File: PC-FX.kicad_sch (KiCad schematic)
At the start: 60 parts, among them CN101 Conn_01x18_Socket, CN102 Conn_01x10_Pin, CN103 Conn_01x07_Pin, CN104 Conn_01x06_Pin, CN105 Conn_01x03_Socket, IC106 BA4510F, IC108 BA4510F, Q101 PNP

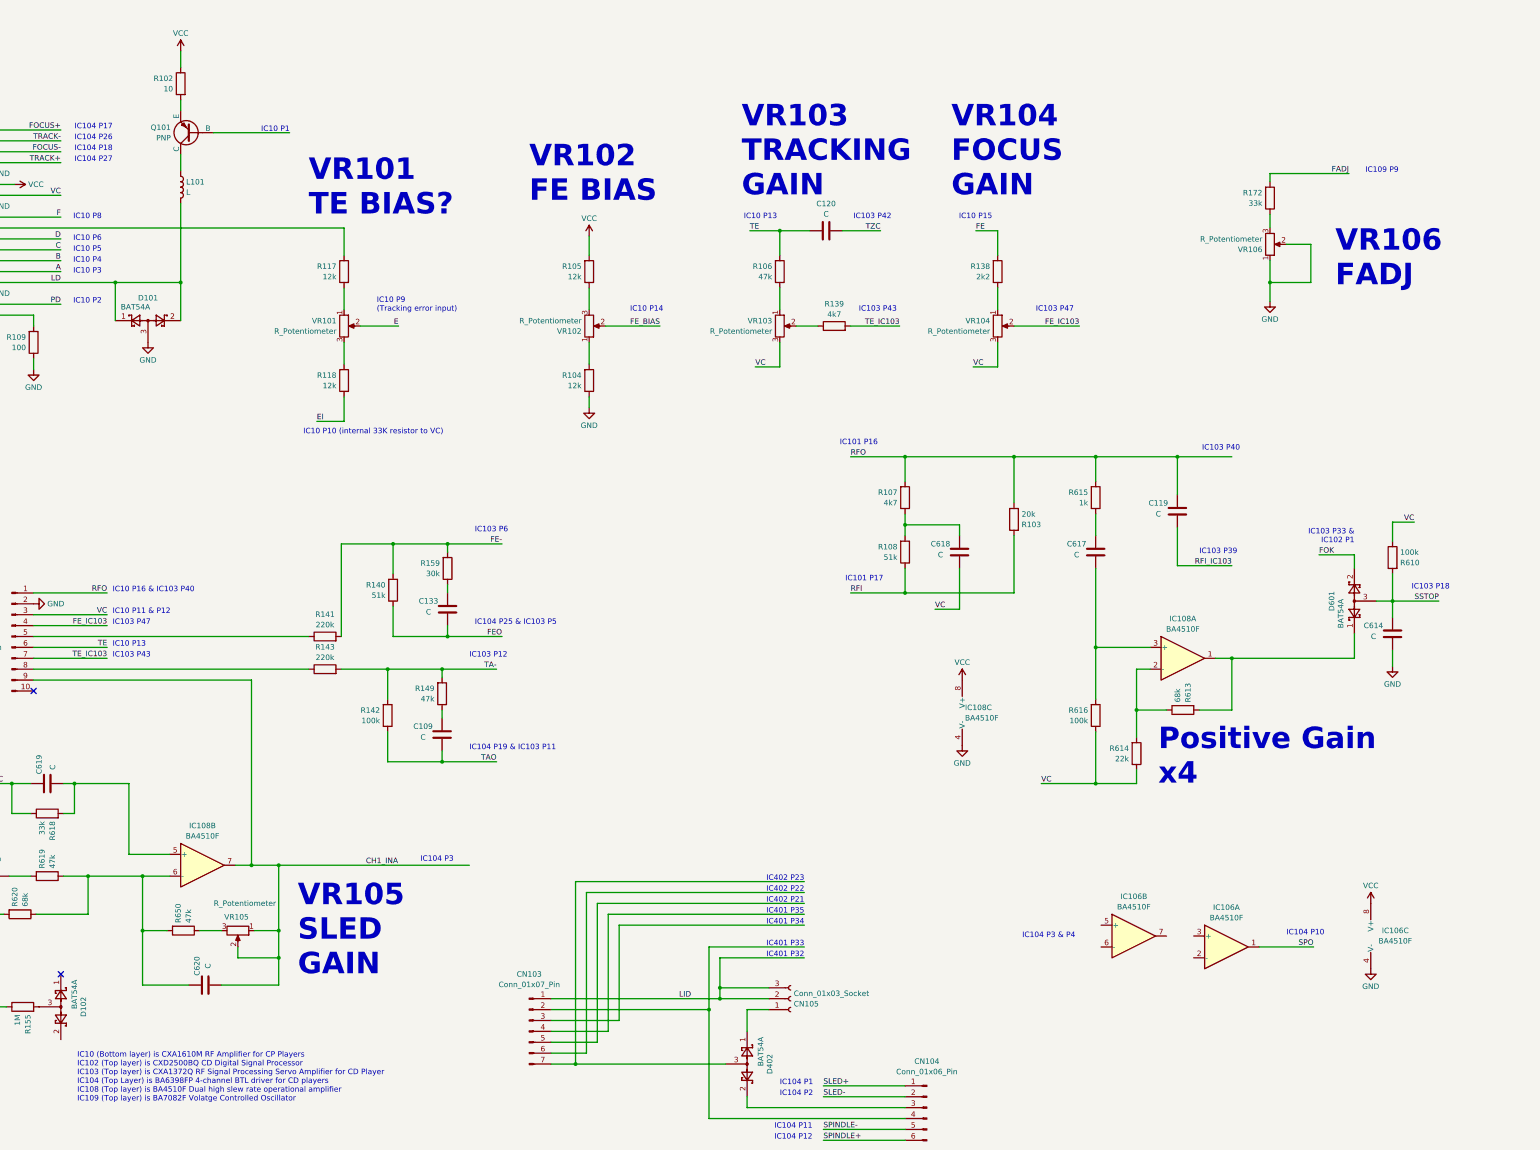
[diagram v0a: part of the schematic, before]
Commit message: Update that includes Frequency adjustment.
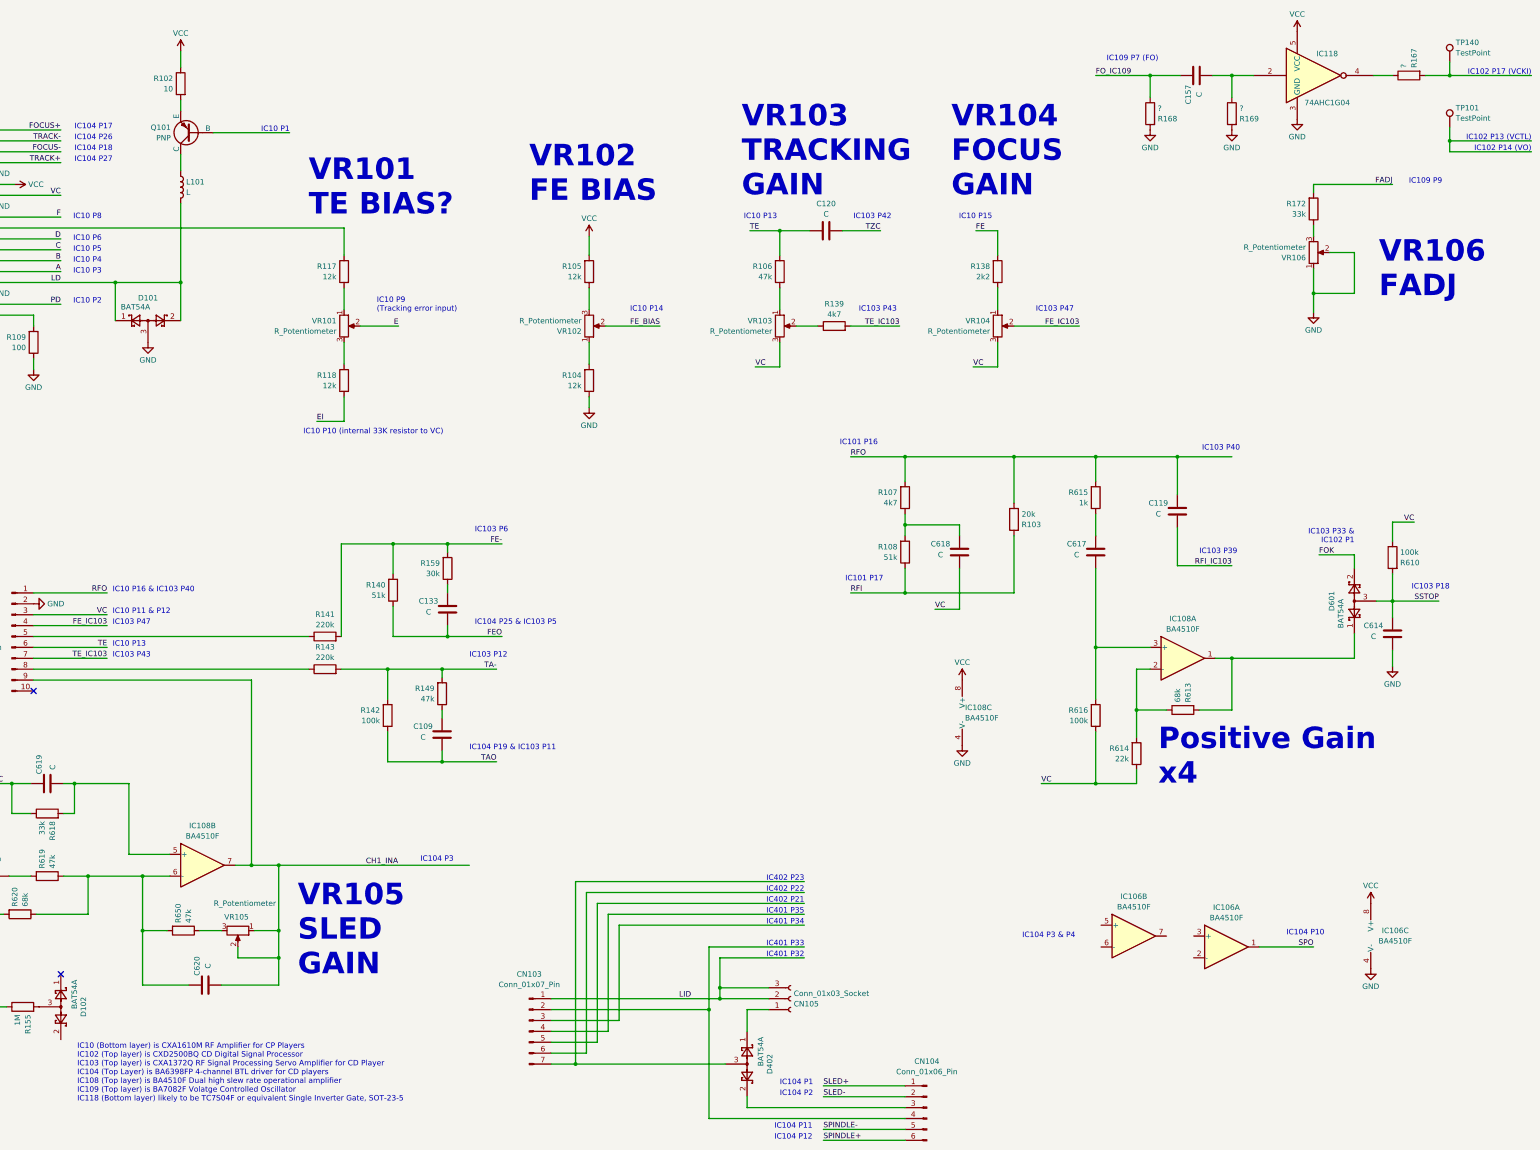
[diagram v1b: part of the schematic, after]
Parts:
- added C157: C, symbol Device:C
- added IC118: 74AHC1G04, symbol 74xGxx:74AHC1G04
- added R167, R168, R169: ?, symbol Device:R
- added TP101, TP140: TestPoint, symbol Connector:TestPoint
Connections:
- net GND: now also IC118.3 (GND), R168.2, R169.2
- net VCC: now also IC118.5 (VCC)
- new net: C157.2, IC118.2, R169.1
- new net: R167.2, TP140.1
- new net: IC118.4, R167.1
- new net FO_IC109: C157.1, R168.1
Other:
- note added: "IC10 (Bottom layer) is CXA1610M RF Amplifier for CP Players IC102 (Top layer) is CXD2500BQ CD Digital Signal Processor IC103 (Top layer) is CXA1372Q RF Signal Processing Servo Amplifier for CD Player IC104 (Top Layer) is BA6398FP 4-channel BTL driver for CD players IC108 (Top layer) is BA4510F Dual high slew rate operational amplifier IC109 (Top layer) is BA7082F Volatge Controlled Oscillator IC1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"
- note added: "IC102 P13 (VCTL)"
- note added: "IC102 P14 (VO)"
- note added: "IC102 P17 (VCKI)"
- note added: "IC109 P7 (FO)"
- note removed: "IC10 (Bottom layer) is CXA1610M RF Amplifier for CP Players IC102 (Top layer) is CXD2500BQ CD Digital Signal Processor IC103 (Top layer) is CXA1372Q RF Signal Processing Servo Amplifier for CD Player IC104 (Top Layer) is BA6398FP 4-channel BTL driver for CD players IC108 (Top layer) is BA4510F Dual high slew rate operational amplifier IC109 (Top layer) is BA7082F Volatge Controlled Oscillator"
- moved on the sheet: R172, VR106
